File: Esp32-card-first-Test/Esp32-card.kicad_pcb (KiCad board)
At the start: 2 copper layers, 93 x 85 mm, 22 parts, among them J1 Conn_01x14_Socket, J10 Conn_01x02_Pin, J11 Conn_01x02_Pin, J12 Conn_01x05_Pin, J13 Conn_01x02_Pin, J14 Conn_01x06_Pin, J2 Conn_01x02_Pin, J3 Conn_01x02_Pin, J4 Conn_01x03_Pin, J5 Conn_01x03_Pin, J6 Conn_01x02_Pin, J8 Conn_01x06_Pin, J9 Conn_01x05_Pin, U1 74HC595, U2 74HC595, U4 74HC4051

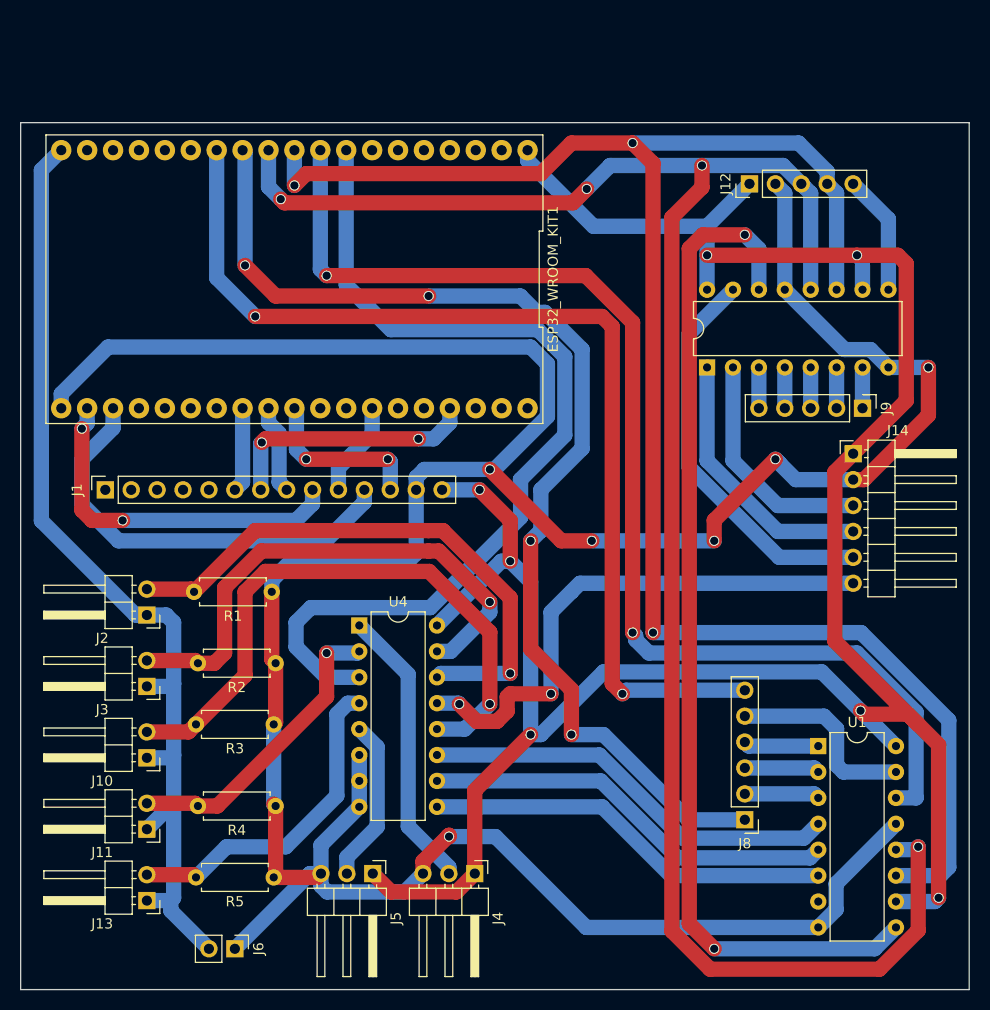
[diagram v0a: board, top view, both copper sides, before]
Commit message: add and congif Visual studio code projet
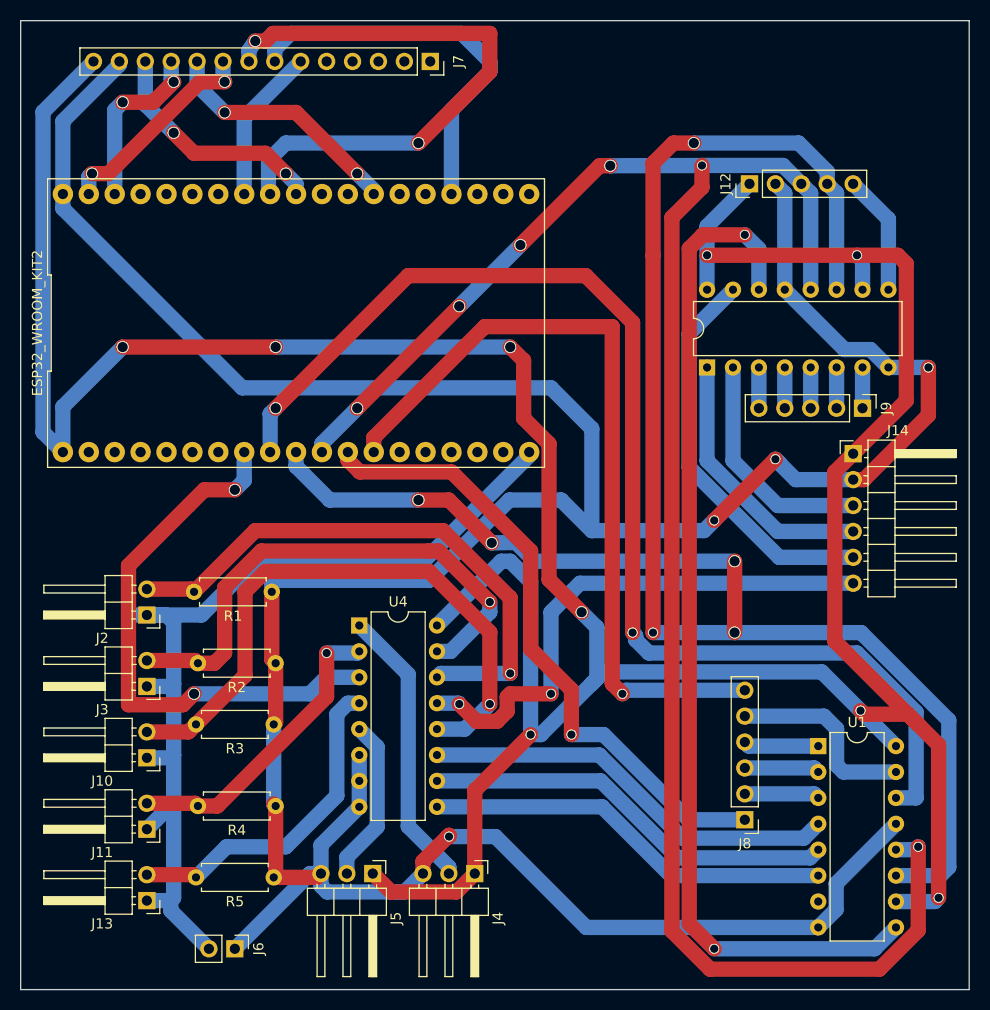
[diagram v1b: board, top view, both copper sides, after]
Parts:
- removed ESP32_WROOM_KIT1: ~, MyEsp32Library:Esp32_Wroom32_DevKit
- removed J1: Conn_01x14_Socket, Connector_PinSocket_2.54mm:PinSocket_1x14_P2.54mm_Vertical
- added ESP32_WROOM_KIT2: ~, MyEsp32Library:Esp32_Wroom32_DevKit, F.Cu at (143.0, 61.6)
- added J7: Conn_01x14_Socket, Connector_PinSocket_2.54mm:PinSocket_1x14_P2.54mm_Vertical, F.Cu at (156.2, 36.0)
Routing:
- net 3v3: track 244.5 -> 340.0 mm, vias 7 -> 9
- net SCK: track 0.00 -> 57.9 mm, vias 0 -> 2
- net M2_Pin_EN: track 109.8 -> 62.5 mm, vias 4 -> 1
- net Net-(ESP32_WROOM_KIT1-GPIO22): track 42.6 -> 0.00 mm
- net LED: track 0.00 -> 38.6 mm
- net Analog_Pin1: track 91.2 -> 55.0 mm, vias 0 -> 2
- net Net-(ESP32_WROOM_KIT1-GPIO23): track 35.3 -> 0.00 mm, vias 2 -> 0
- net Net-(ESP32_WROOM_KIT1-GPIO15): track 25.3 -> 0.00 mm, vias 2 -> 0
- net DC: track 0.00 -> 24.3 mm, vias 0 -> 2
- net M1_Pin_EN: track 101.8 -> 77.9 mm, vias 2 -> 1
- net CS: track 0.00 -> 23.2 mm, vias 0 -> 2
- net MOSI: track 0.00 -> 20.9 mm, vias 0 -> 2
- net RESET: track 0.00 -> 17.3 mm, vias 0 -> 2
- net Net-(ESP32_WROOM_KIT1-GPIO5): track 16.6 -> 0.00 mm, vias 2 -> 0
- net MISO: track 0.00 -> 15.3 mm
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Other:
- board size 93 x 85 mm -> 93 x 95 mm
